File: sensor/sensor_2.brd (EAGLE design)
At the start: 100 x 80 mm, 29 parts, among them IC1 INA116U, IC3 LT6230LT6010(MOD12.2013), T1 BC849SMD, T2 BC849SMD

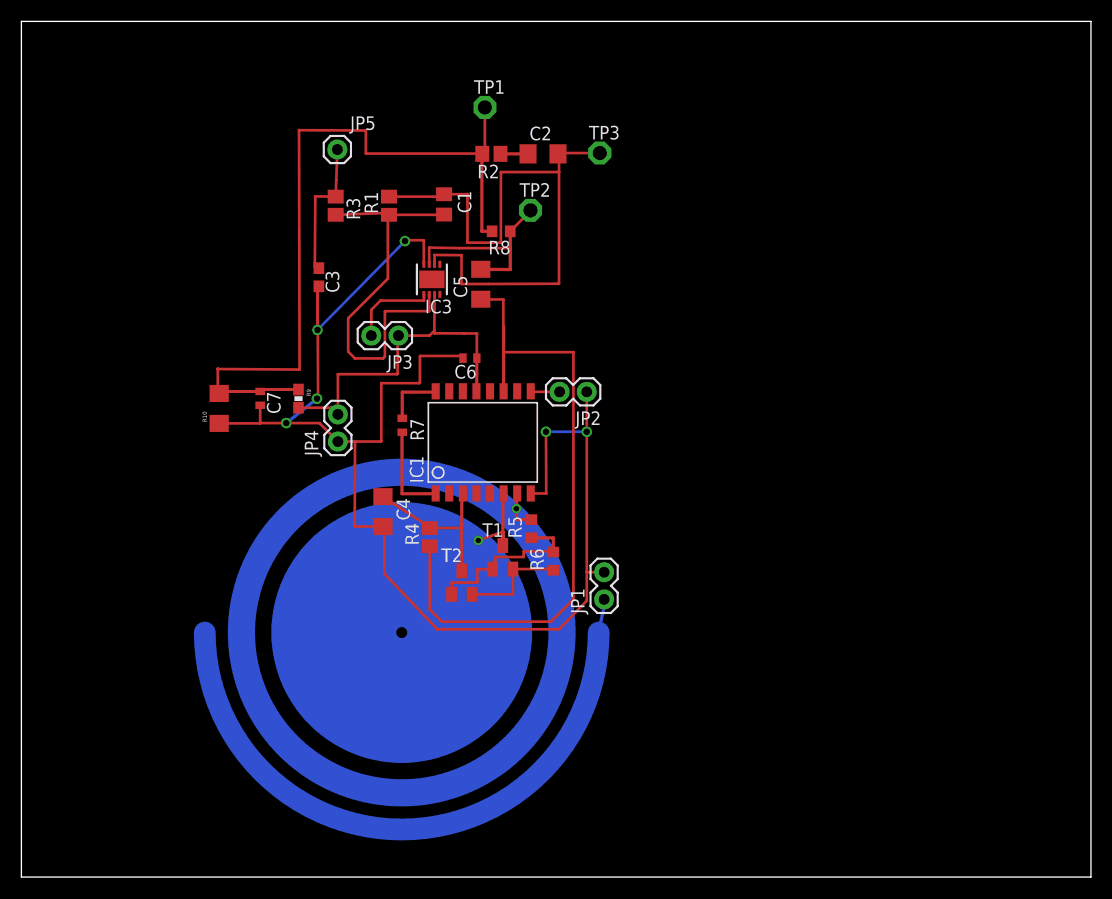
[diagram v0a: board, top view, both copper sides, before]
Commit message: // added a trace restricted area for sensor plane // reorganized parts for optimal space and routing
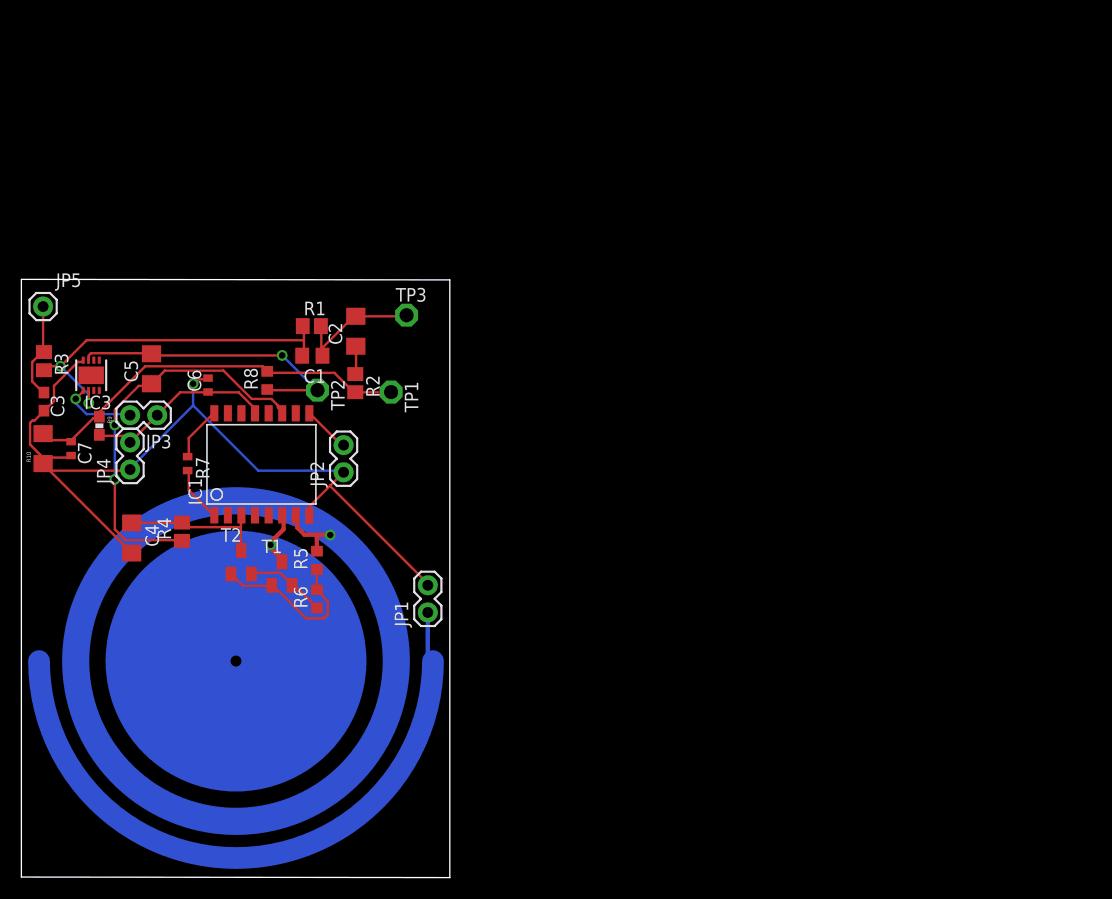
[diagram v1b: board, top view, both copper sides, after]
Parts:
- moved IC3 33.1 mm to (6.53, 46.9)
- moved C5 31.8 mm to (12.2, 47.5)
- moved JP5 31.2 mm to (2.03, 53.3)
- moved R3 30.9 mm to (2.11, 48.2)
- moved C3 28.2 mm to (2.11, 44.5)
- moved TP1 28.0 mm to (34.6, 45.3), turned to 270 degrees
- moved TP2 26.1 mm to (27.7, 45.5), turned to 270 degrees
- moved R8 25.9 mm to (23.0, 46.4), turned to 90 degrees
- moved R2 24.9 mm to (31.2, 46.2), turned to 270 degrees
- moved C6 24.6 mm to (17.4, 46.0), turned to 90 degrees
- moved C2 24.1 mm to (31.3, 51.0), turned to 90 degrees
- moved JP2 23.9 mm to (30.1, 37.8), turned to 90 degrees
- moved JP3 23.8 mm to (12.7, 43.2)
- moved C4 23.6 mm to (10.3, 31.7)
- moved TP3 23.6 mm to (36.0, 52.5)
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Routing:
- net AGND: track 137.0 -> 83.2 mm, vias 6 -> 1
- net N$9: track 58.3 -> 12.8 mm
- net 1.5V: track 79.4 -> 37.1 mm
- net N$3: track 61.2 -> 36.9 mm, vias 0 -> 2
- net 5V: track 33.5 -> 17.9 mm
- net N$10: track 18.2 -> 28.1 mm, vias 0 -> 1
- net OUTPUT: track 13.4 -> 9.06 mm
- net N$11: track 38.5 -> 34.2 mm, vias 0 -> 2
- net N$1: track 8.95 -> 5.29 mm
- net IN+: track 8.63 -> 5.28 mm, vias 1 -> 0
- net IN-: track 16.1 -> 13.7 mm
- net RESET-: track 10.1 -> 7.77 mm
- net G+: track 3.83 -> 6.07 mm, vias 1 -> 0
- net REF: track 2.71 -> 4.60 mm
- net GND_PLANE: track 40.1 -> 41.9 mm
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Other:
- board size 100 x 80 mm -> 40.1 x 55.9 mm
